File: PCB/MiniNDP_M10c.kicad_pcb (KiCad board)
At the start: 2 copper layers, 58 x 31 mm, 21 parts, among them J1 Conn_02x20_Odd_Even, U1 AS6C8008_TSOPII, U2 HC238, U3 HC4040, U4 ABT841

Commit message: fix tssop-24 model, update cover models
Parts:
- N1: value MiniNDP_Cover_M10 -> MiniNDP_Cover_M10c; footprint 000_LOCAL:MiniNDP_Cover_M10 -> 000_LOCAL:MiniNDP_Cover_M10c
- U4: footprint 000_LOCAL:TSSOP-24_4.4x7.8mm_P0.65mm -> 000_LOCAL:TSSOP-24

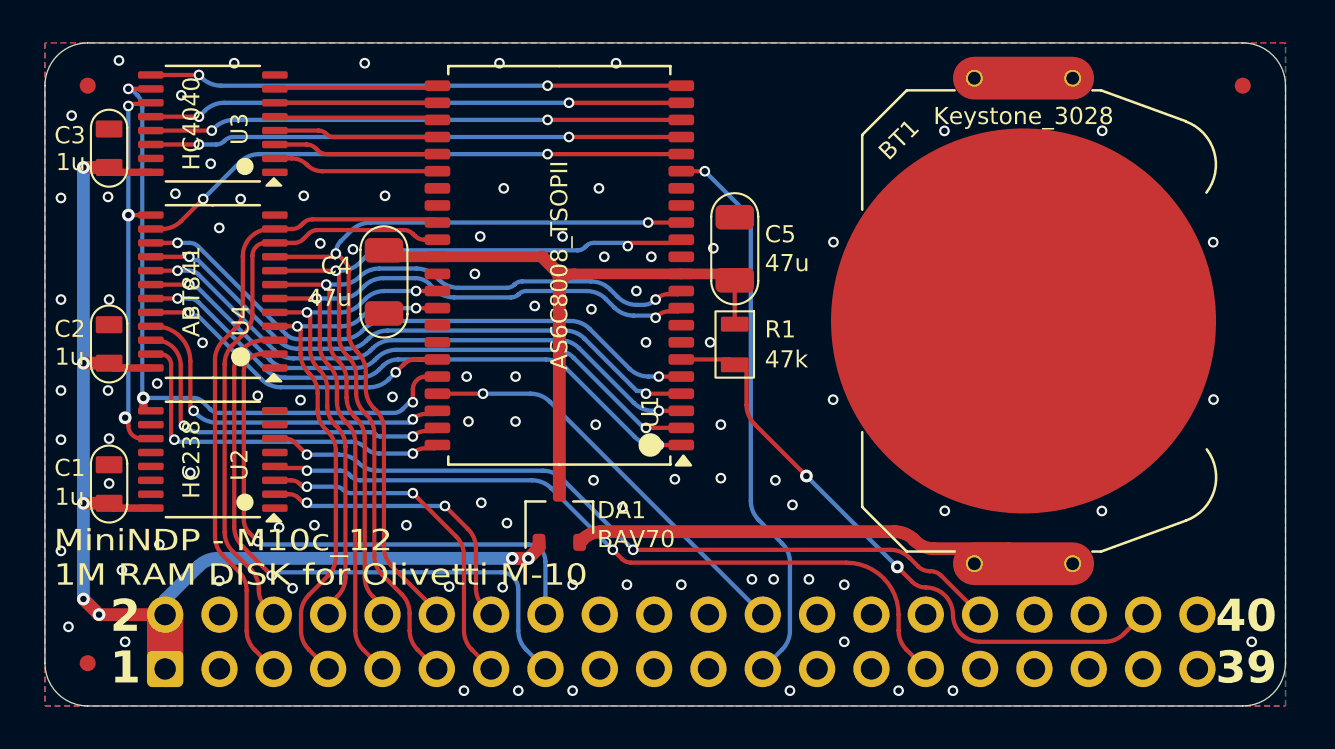
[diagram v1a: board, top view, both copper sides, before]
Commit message: M10c compact pcb & cover a little smaller & symmetrical
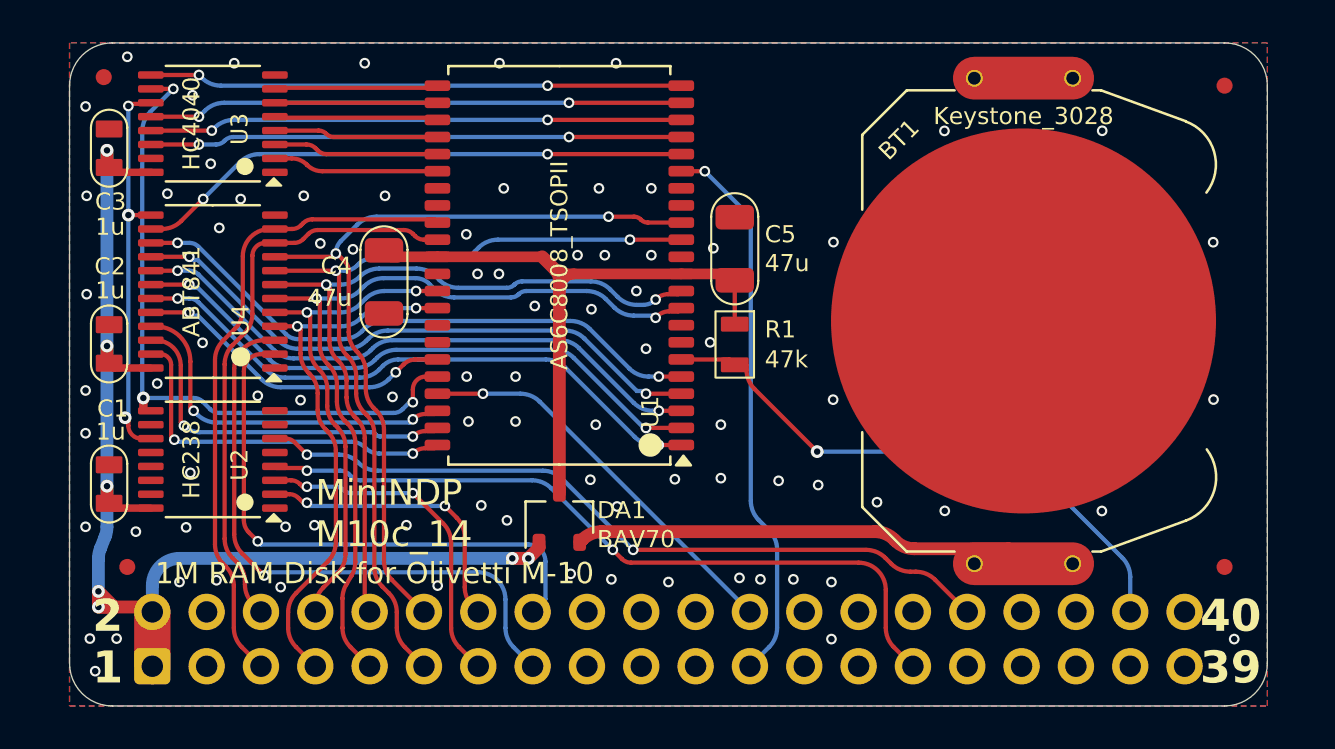
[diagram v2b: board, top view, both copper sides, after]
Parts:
- added F3: Fiducial_0.75_1.5, 000_LOCAL:Fiducial_0.75_1.5, F.Cu at (177.3, 111.5)
- N1: value MiniNDP_Cover_M10c -> MiniNDP_Cover_M10compact; footprint 000_LOCAL:MiniNDP_Cover_M10c -> 000_LOCAL:MiniNDP_Cover_M10compact
- moved F3 4.87 mm to (126.0, 111.5)
- moved F3 0.85 mm to (125.0, 88.6)
- moved F3 0.85 mm to (177.3, 89.0)
- moved J1 0.61 mm to (127.2, 116.2)
- moved N1 0.15 mm to (151.3, 102.5)
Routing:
- net /RAMRST: track 29.0 -> 27.4 mm, vias 2 -> 1
- net VBUS: track 57.7 -> 58.9 mm
- net /BUS_A11: track 29.2 -> 28.4 mm
- net /(A): track 36.0 -> 35.3 mm
- net /~{RD}: track 19.4 -> 18.8 mm
- net /AD7: track 39.7 -> 39.2 mm
- net GND: vias 92 -> 85
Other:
- board size 58 x 31 mm -> 56 x 31 mm
- board text added: "${TITLE} ${REVISION}"
- board text added: "1M RAM Disk for Olivetti M-10"
- board text removed: "${TITLE} - ${REVISION} 1M RAM DISK for Olivetti M-10"
